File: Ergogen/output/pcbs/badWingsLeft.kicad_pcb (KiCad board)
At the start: 2 copper layers, 147.6 x 109.7 mm, 154 parts

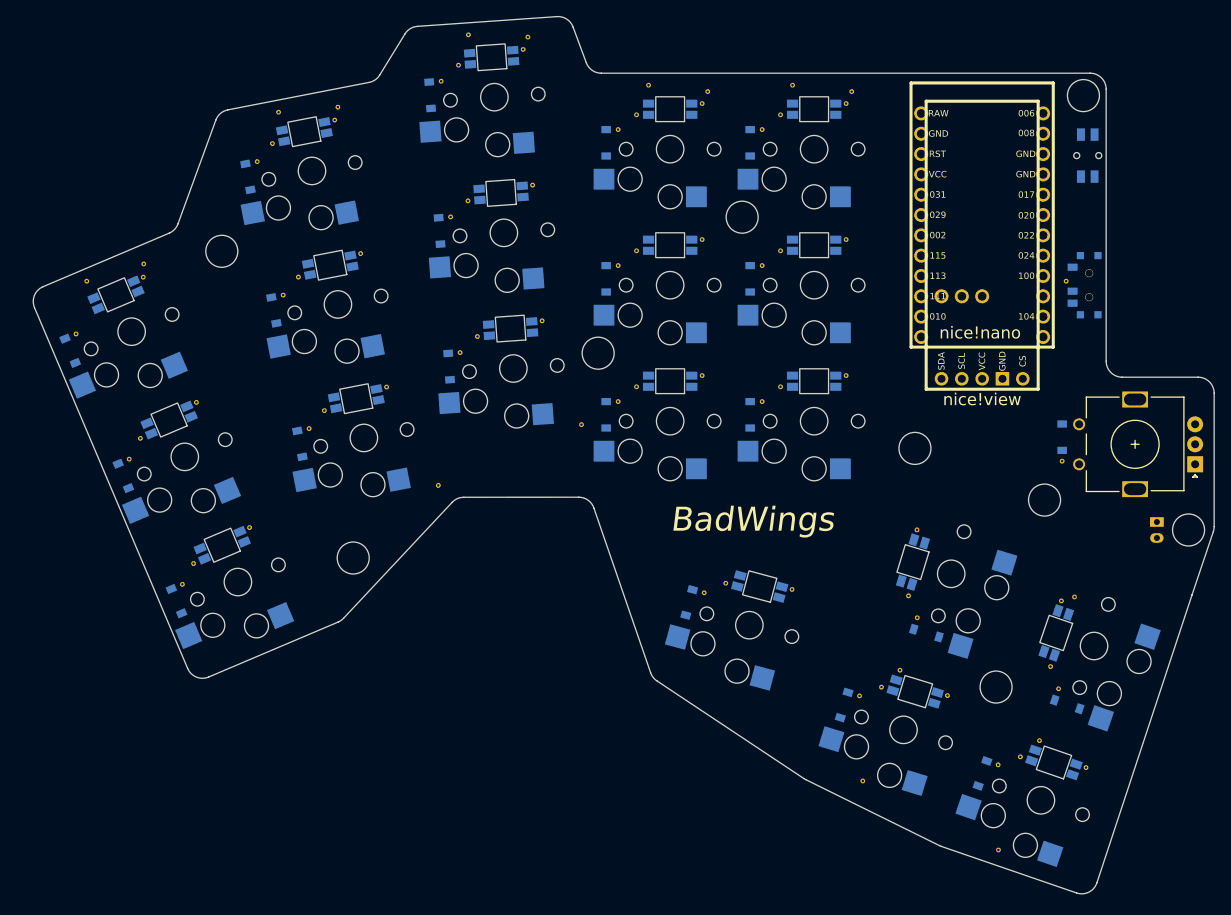
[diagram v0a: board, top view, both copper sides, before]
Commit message: Left board traced
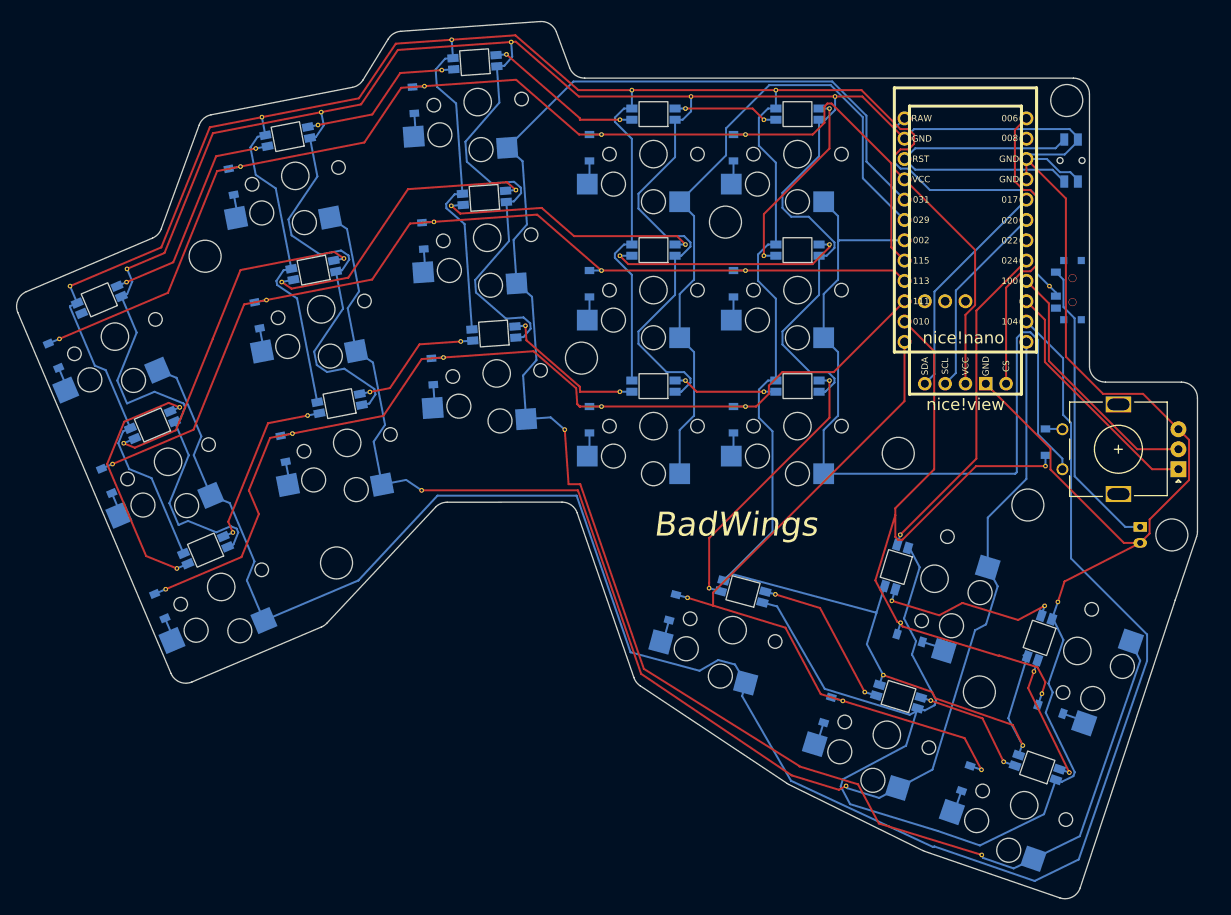
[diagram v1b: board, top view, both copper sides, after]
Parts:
- removed the ? at (172.9, 197.2)
- removed the ? at (92.6, 181.1)
- removed the ? at (76.1, 142.8)
- removed the ? at (141.2, 138.5)
- removed the ? at (197.0, 177.6)
- removed the ? at (123.2, 155.5)
- removed the ? at (162.8, 167.4)
- removed the ? at (179.0, 173.9)
- removed the ? at (183.8, 123.3)
- removed the REF** at (71.2, 184.4)
- removed the REF** at (125.7, 161.5)
- removed the REF** at (125.7, 144.5)
- removed the REF** at (125.7, 127.5)
- removed the REF** at (143.7, 161.5)
- removed the REF** at (143.7, 144.5)
- removed the REF** at (143.7, 127.5)
- removed the REF** at (136.4, 185.4)
- removed the REF** at (155.8, 198.3)
- removed the REF** at (163.1, 188.6)
- removed the REF** at (173.2, 207.0)
- removed the REF** at (64.6, 168.7)
- removed the REF** at (180.7, 197.4)
- removed the REF** at (72.6, 181.8)
- removed the REF** at (66.0, 166.1)
- removed the REF** at (89.0, 162.7)
- removed the REF** at (85.7, 146.0)
- removed the REF** at (82.5, 129.3)
- removed the REF** at (108.1, 153.4)
- removed the REF** at (106.9, 136.5)
- removed the REF** at (105.7, 119.5)
- removed the REF** at (128.0, 159.7)
- removed the REF** at (57.9, 153.1)
- removed the REF** at (128.0, 142.7)
- removed the REF** at (128.0, 125.7)
- removed the REF** at (146.0, 159.7)
- removed the REF** at (146.0, 142.7)
- removed the REF** at (146.0, 125.7)
- removed the REF** at (139.1, 184.3)
- removed the REF** at (158.6, 197.2)
- removed the REF** at (162.0, 185.8)
- removed the REF** at (176.0, 206.0)
- removed the REF** at (179.7, 194.7)
- removed the REF** at (87.0, 164.9)
- removed the REF** at (79.6, 177.3)
- removed the REF** at (73.0, 161.6)
- removed the REF** at (66.3, 146.0)
- removed the REF** at (96.7, 159.7)
- removed the REF** at (93.5, 143.0)
- removed the REF** at (90.2, 126.4)
- removed the REF** at (116.2, 151.4)
- removed the REF** at (115.0, 134.5)
- removed the REF** at (113.8, 117.5)
- removed the REF** at (136.2, 158.3)
- removed the REF** at (83.8, 148.2)
- removed the REF** at (136.2, 141.3)
- removed the REF** at (136.2, 124.3)
- removed the REF** at (154.2, 158.3)
- removed the REF** at (154.2, 141.3)
- removed the REF** at (154.2, 124.3)
- removed the REF** at (147.4, 185.0)
- removed the REF** at (166.8, 198.3)
- removed the REF** at (163.0, 177.6)
- removed the REF** at (184.2, 207.3)
- removed the REF** at (181.1, 186.5)
- removed the REF** at (80.6, 131.5)
- removed the REF** at (66.4, 144.3)
- removed the REF** at (90.6, 124.7)
- removed the REF** at (114.4, 116.0)
- removed the REF** at (136.9, 122.8)
- removed the REF** at (154.9, 122.8)
- removed the REF** at (59.3, 146.5)
- removed the REF** at (83.2, 125.4)
- removed the REF** at (107.0, 115.7)
- removed the REF** at (129.5, 122.0)
- removed the REF** at (147.5, 122.0)
- removed the REF** at (105.9, 155.4)
- removed the REF** at (181.7, 146.5)
- removed the REF** at (181.2, 169.0)
- removed the REF** at (103.2, 172.0)
- removed the REF** at (156.3, 209.0)
- removed the REF** at (121.1, 164.4)
- removed the REF** at (173.2, 217.6)
- removed the REF** at (160.9, 195.1)
- removed the REF** at (178.3, 203.9)
- removed the REF** at (182.7, 186.0)
- removed the REF** at (104.7, 138.5)
- removed the REF** at (103.6, 121.5)
- added ?: , HOLE_M2_TH, F.Cu at (160.7, 168.0)
- added ?: , HOLE_M2_TH, F.Cu at (181.8, 123.9)
- added ?: , HOLE_M2_TH, F.Cu at (176.9, 174.5)
- added ?: , HOLE_M2_TH, F.Cu at (194.9, 178.2)
- added ?: , HOLE_M2_TH, F.Cu at (90.5, 181.7)
- added ?: , HOLE_M2_TH, F.Cu at (74.0, 143.4)
- added ?: , HOLE_M2_TH, F.Cu at (139.1, 139.1)
- added ?: , HOLE_M2_TH, F.Cu at (121.1, 156.1)
- added ?: , HOLE_M2_TH, F.Cu at (170.8, 197.8)
- added REF**: VIA-0.6mm, VIA-0.6mm, F.Cu at (134.8, 123.4)
- added REF**: VIA-0.6mm, VIA-0.6mm, F.Cu at (152.1, 158.9)
- added REF**: VIA-0.6mm, VIA-0.6mm, F.Cu at (103.8, 156.0)
- added REF**: VIA-0.6mm, VIA-0.6mm, F.Cu at (180.6, 186.6)
- added REF**: VIA-0.6mm, VIA-0.6mm, F.Cu at (152.1, 141.9)
- added REF**: VIA-0.6mm, VIA-0.6mm, F.Cu at (78.5, 132.2)
- added REF**: VIA-0.6mm, VIA-0.6mm, F.Cu at (112.9, 135.1)
- added REF**: VIA-0.6mm, VIA-0.6mm, F.Cu at (83.6, 146.6)
- added REF**: VIA-0.6mm, VIA-0.6mm, F.Cu at (145.4, 122.6)
- added REF**: VIA-0.6mm, VIA-0.6mm, F.Cu at (125.9, 126.3)
- added REF**: VIA-0.6mm, VIA-0.6mm, F.Cu at (158.8, 195.7)
- added REF**: VIA-0.6mm, VIA-0.6mm, F.Cu at (134.3, 186.1)
- added REF**: VIA-0.6mm, VIA-0.6mm, F.Cu at (171.1, 207.6)
- added REF**: VIA-0.6mm, VIA-0.6mm, F.Cu at (141.6, 145.2)
- added REF**: VIA-0.6mm, VIA-0.6mm, F.Cu at (88.6, 125.4)
- added REF**: VIA-0.6mm, VIA-0.6mm, F.Cu at (179.0, 187.1)
- added REF**: VIA-0.6mm, VIA-0.6mm, F.Cu at (77.5, 177.9)
- added REF**: VIA-0.6mm, VIA-0.6mm, F.Cu at (137.0, 184.9)
- added REF**: VIA-0.6mm, VIA-0.6mm, F.Cu at (156.5, 197.9)
- added REF**: VIA-0.6mm, VIA-0.6mm, F.Cu at (134.1, 158.9)
- added REF**: VIA-0.6mm, VIA-0.6mm, F.Cu at (143.9, 160.3)
- added REF**: VIA-0.6mm, VIA-0.6mm, F.Cu at (111.7, 118.1)
- added REF**: VIA-0.6mm, VIA-0.6mm, F.Cu at (101.1, 172.6)
- added REF**: VIA-0.6mm, VIA-0.6mm, F.Cu at (94.6, 160.3)
- added REF**: VIA-0.6mm, VIA-0.6mm, F.Cu at (160.9, 178.2)
- added REF**: VIA-0.6mm, VIA-0.6mm, F.Cu at (182.1, 207.9)
- added REF**: VIA-0.6mm, VIA-0.6mm, F.Cu at (86.9, 163.3)
- added REF**: VIA-0.6mm, VIA-0.6mm, F.Cu at (134.1, 141.9)
- added REF**: VIA-0.6mm, VIA-0.6mm, F.Cu at (101.5, 122.1)
- added REF**: VIA-0.6mm, VIA-0.6mm, F.Cu at (103.6, 120.1)
- added REF**: VIA-0.6mm, VIA-0.6mm, F.Cu at (164.8, 198.9)
- added REF**: VIA-0.6mm, VIA-0.6mm, F.Cu at (64.2, 146.6)
- added REF**: VIA-0.6mm, VIA-0.6mm, F.Cu at (178.6, 198.1)
- added REF**: VIA-0.6mm, VIA-0.6mm, F.Cu at (119.0, 165.0)
- added REF**: VIA-0.6mm, VIA-0.6mm, F.Cu at (64.3, 145.0)
- added REF**: VIA-0.6mm, VIA-0.6mm, F.Cu at (123.6, 145.2)
- added REF**: VIA-0.6mm, VIA-0.6mm, F.Cu at (176.3, 204.5)
- added REF**: VIA-0.6mm, VIA-0.6mm, F.Cu at (81.7, 148.9)
- added REF**: VIA-0.6mm, VIA-0.6mm, F.Cu at (161.0, 189.2)
- added REF**: VIA-0.6mm, VIA-0.6mm, F.Cu at (179.1, 169.6)
- added REF**: VIA-0.6mm, VIA-0.6mm, F.Cu at (173.9, 206.6)
- added REF**: VIA-0.6mm, VIA-0.6mm, F.Cu at (152.8, 123.4)
- added REF**: VIA-0.6mm, VIA-0.6mm, F.Cu at (125.9, 143.3)
- added REF**: VIA-0.6mm, VIA-0.6mm, F.Cu at (152.1, 124.9)
- added REF**: VIA-0.6mm, VIA-0.6mm, F.Cu at (143.9, 143.3)
- added REF**: VIA-0.6mm, VIA-0.6mm, F.Cu at (104.9, 116.3)
- added REF**: VIA-0.6mm, VIA-0.6mm, F.Cu at (141.6, 162.2)
- added REF**: VIA-0.6mm, VIA-0.6mm, F.Cu at (171.1, 218.2)
- added REF**: VIA-0.6mm, VIA-0.6mm, F.Cu at (114.1, 152.1)
- added REF**: VIA-0.6mm, VIA-0.6mm, F.Cu at (145.3, 185.6)
- added REF**: VIA-0.6mm, VIA-0.6mm, F.Cu at (88.2, 127.0)
- added REF**: VIA-0.6mm, VIA-0.6mm, F.Cu at (154.2, 209.6)
- added REF**: VIA-0.6mm, VIA-0.6mm, F.Cu at (159.9, 186.4)
- added REF**: VIA-0.6mm, VIA-0.6mm, F.Cu at (69.1, 185.0)
- added REF**: VIA-0.6mm, VIA-0.6mm, F.Cu at (127.4, 122.6)
- added REF**: VIA-0.6mm, VIA-0.6mm, F.Cu at (104.8, 137.1)
- added REF**: VIA-0.6mm, VIA-0.6mm, F.Cu at (179.6, 147.1)
- added REF**: VIA-0.6mm, VIA-0.6mm, F.Cu at (70.5, 182.4)
- added REF**: VIA-0.6mm, VIA-0.6mm, F.Cu at (57.2, 147.1)
- added REF**: VIA-0.6mm, VIA-0.6mm, F.Cu at (123.6, 128.2)
- added REF**: VIA-0.6mm, VIA-0.6mm, F.Cu at (125.9, 160.3)
- added REF**: VIA-0.6mm, VIA-0.6mm, F.Cu at (177.6, 195.3)
- added REF**: VIA-0.6mm, VIA-0.6mm, F.Cu at (62.5, 169.4)
- added REF**: VIA-0.6mm, VIA-0.6mm, F.Cu at (112.3, 116.6)
- added REF**: VIA-0.6mm, VIA-0.6mm, F.Cu at (153.8, 199.0)
- added REF**: VIA-0.6mm, VIA-0.6mm, F.Cu at (70.9, 162.3)
- added REF**: VIA-0.6mm, VIA-0.6mm, F.Cu at (102.7, 139.1)
- added REF**: VIA-0.6mm, VIA-0.6mm, F.Cu at (143.9, 126.3)
- added REF**: VIA-0.6mm, VIA-0.6mm, F.Cu at (106.0, 154.0)
- added REF**: VIA-0.6mm, VIA-0.6mm, F.Cu at (81.1, 126.0)
- added REF**: VIA-0.6mm, VIA-0.6mm, F.Cu at (91.4, 143.7)
- added REF**: VIA-0.6mm, VIA-0.6mm, F.Cu at (141.6, 128.2)
- added REF**: VIA-0.6mm, VIA-0.6mm, F.Cu at (85.0, 165.5)
- added REF**: VIA-0.6mm, VIA-0.6mm, F.Cu at (123.6, 162.2)
- added REF**: VIA-0.6mm, VIA-0.6mm, F.Cu at (55.8, 153.7)
- added REF**: VIA-0.6mm, VIA-0.6mm, F.Cu at (80.4, 129.9)
- added REF**: VIA-0.6mm, VIA-0.6mm, F.Cu at (134.1, 124.9)
- added REF**: VIA-0.6mm, VIA-0.6mm, F.Cu at (63.9, 166.8)
- moved LED18 2.18 mm to (160.4, 182.2)
- moved S6 2.18 mm to (85.3, 133.3)
- moved D10 2.18 mm to (122.1, 163.8)
- moved B1 2.18 mm to (182.3, 131.4)
- moved LED13 2.18 mm to (148.1, 159.6)
- moved LED14 2.18 mm to (148.1, 142.6)
- moved LED4 2.18 mm to (90.9, 161.8)
- moved ROT1 2.18 mm to (188.1, 167.5)
- moved S2 2.18 mm to (69.4, 169.1)
- moved LED8 2.18 mm to (109.0, 136.1)
- moved LED11 2.18 mm to (130.1, 142.6)
- moved LED5 2.18 mm to (87.6, 145.1)
- moved S1 2.18 mm to (76.1, 184.7)
- moved S19 2.18 mm to (176.4, 212.0)
- moved S20 2.18 mm to (183.1, 192.7)
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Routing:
- net GND: track 0.00 -> 651.1 mm
- net VCC: track 0.00 -> 464.3 mm
- net P104: track 0.00 -> 246.9 mm
- net P031: track 0.00 -> 226.8 mm
- net P106: track 0.00 -> 185.7 mm
- net P115: track 0.00 -> 148.2 mm
- net P111: track 0.00 -> 127.1 mm
- net P113: track 0.00 -> 125.1 mm
- net P002: track 0.00 -> 107.1 mm
- net P010: track 0.00 -> 94.2 mm
- net P009: track 0.00 -> 92.9 mm
- net P029: track 0.00 -> 84.6 mm
- net LED11: track 0.00 -> 44.9 mm
- net RST: track 0.00 -> 42.1 mm
- net P024: track 0.00 -> 42.1 mm
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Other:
- net class Default removed
